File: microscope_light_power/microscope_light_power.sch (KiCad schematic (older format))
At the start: 36 parts, among them J1 MICROUSB, J2 5V175_out, J3 enable_switch, U1 MCP73871-2AA, U2 TPS61090

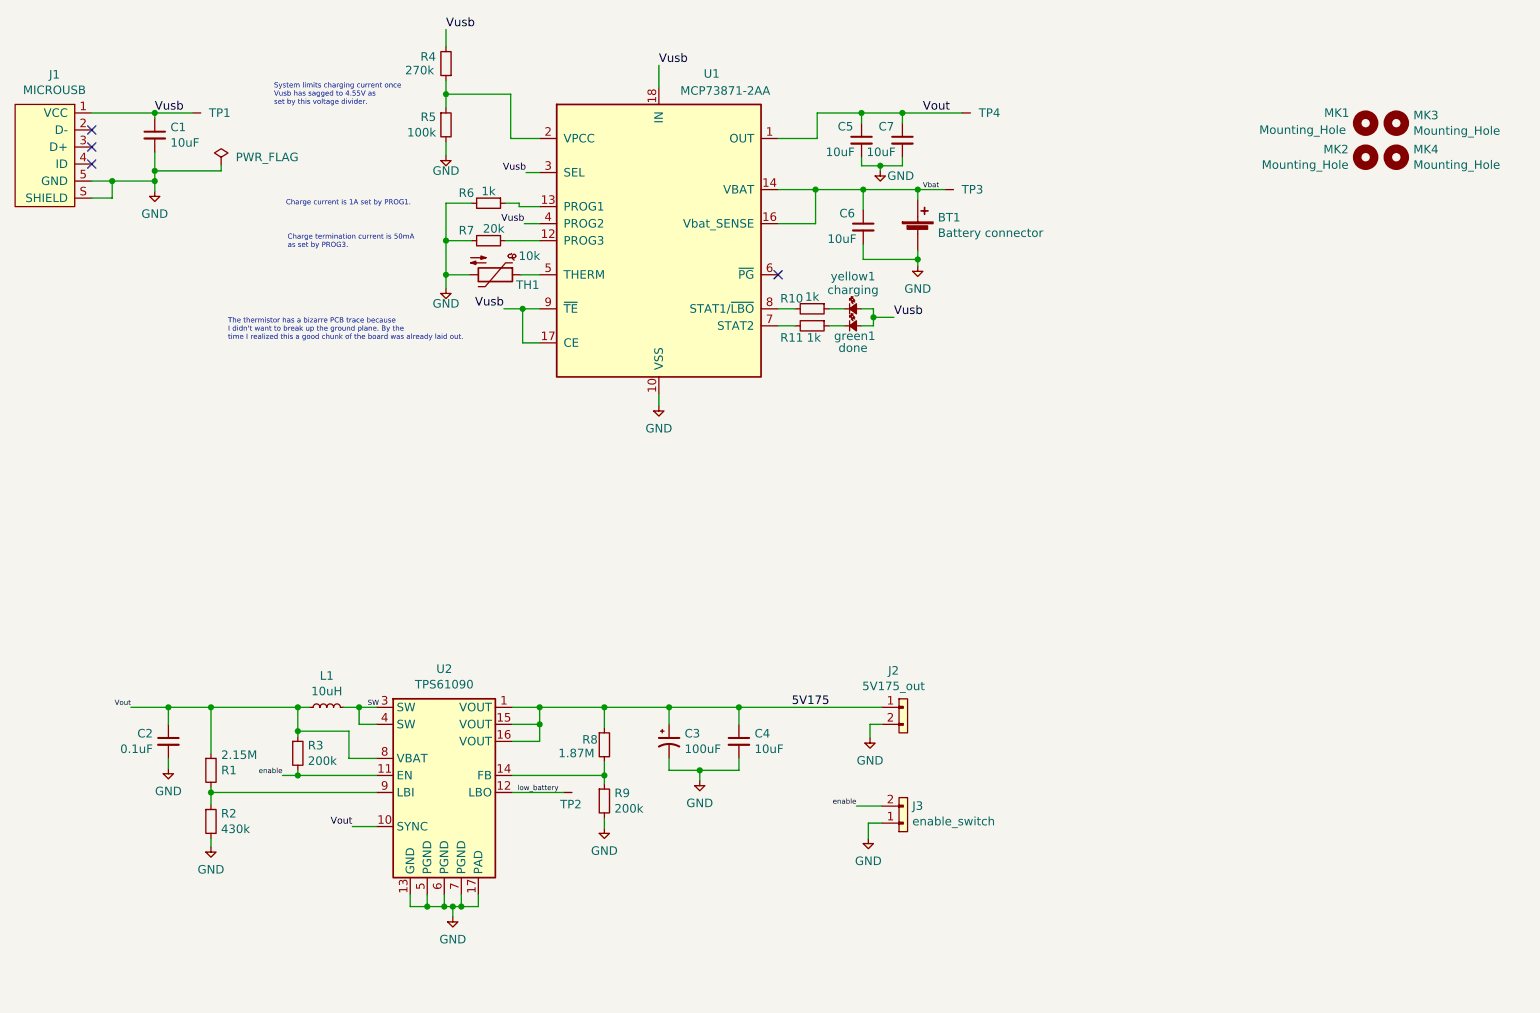
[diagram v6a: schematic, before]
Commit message: Start redoing the layout to fix some major and minor problems with this design: * The SMPS output filter caps are way too far away from the IC. This   keeps killing the internal MOSFET which fails as a short to ground   causing rapid heating and will quickly kill the battery. * The connectors weren't in very good locations. * The PCB is quite a lot bigger than it needs to be. The next rev will   a fun experiment in minituarizing this PCB! * Switch from test pads to test /throughholes/ that are a reasonable   to solder to. * Will add a second pad so the On/Off switch can be switched to normally   on or normally off.
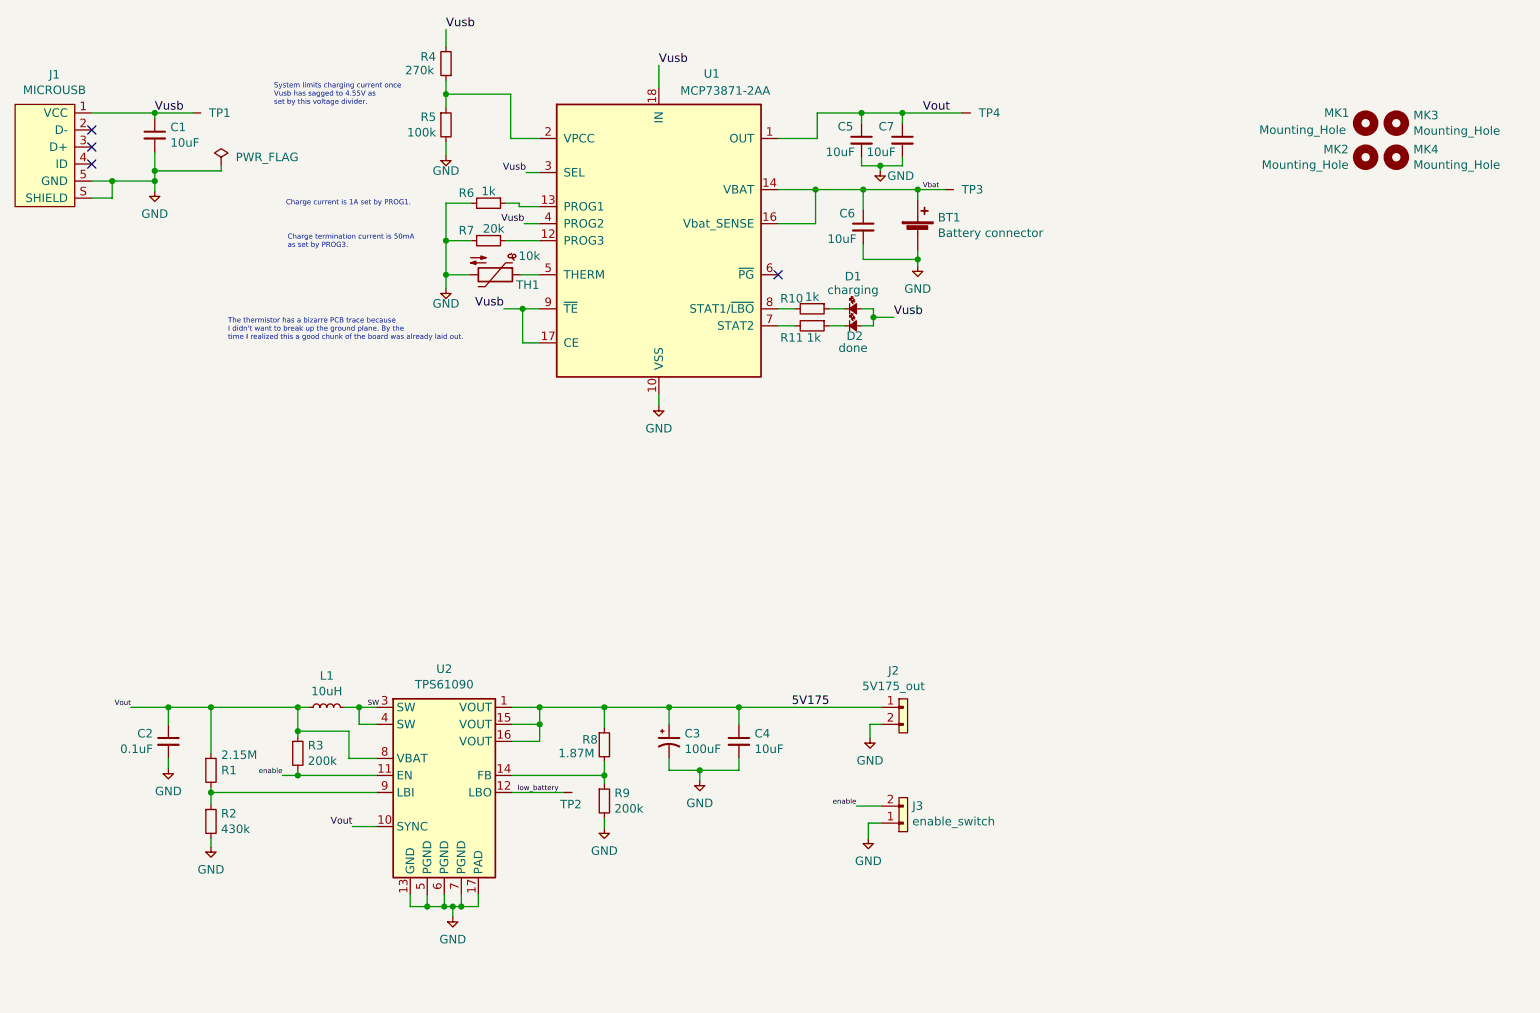
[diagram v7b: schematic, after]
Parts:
- TP1, TP3, TP4: footprint agg:TESTPAD -> Measurement_Points:Measurement_Point_Round-TH_Big
- TP2: footprint Measurement_Points:Measurement_Point_Round-TH_Small -> Measurement_Points:Measurement_Point_Round-TH_Big
- renumbered yellow1 to D1, green1 to D2
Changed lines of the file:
@@
 Vusb
 $Comp
-L agg-kicad:LED yellow1
+L agg-kicad:LED D1
 U 1 1 59DA5C71
 P 6050 2560
-F 0 "yellow1" H 6100 2750 50  0000 C CNN
+F 0 "D1" H 6100 2750 50  0000 C CNN
 F 1 "charging" H 6100 2670 50  0000 C CNN
 F 2 "LEDs:LED_0603_HandSoldering" H 6050 2560 50  0001 C CNN
@@
 $EndComp
 $Comp
-L agg-kicad:LED green1
+L agg-kicad:LED D2
 U 1 1 59DA7F2A
 P 6050 2660
-F 0 "green1" H 6110 2600 50  0000 C CNN
+F 0 "D2" H 6110 2600 50  0000 C CNN
 F 1 "done" H 6100 2530 50  0000 C CNN
 F 2 "LEDs:LED_0603_HandSoldering" H 6050 2660 50  0001 C CNN
@@
 $EndComp
 Wire Wire Line
-	1630 1410 2220 1410
+	1630 1410 2000 1410
 Wire Wire Line
 	2000 1410 2000 1440
 Wire Wire Line
-	1630 1810 2000 1810
-Wire Wire Line
-	2000 1640 2000 1870
+	1630 1810 1750 1810
+Wire Wire Line
+	2000 1640 2000 1750
 Wire Wire Line
 	1630 1910 1750 1910
@@
 	4960 1130 4960 1260
 Wire Wire Line
-	3710 1220 3710 1380
+	3710 1220 3710 1300
 Wire Wire Line
 	3710 920  3710 1020
@@
 	4260 1760 4180 1760
 Wire Wire Line
-	5660 1860 6640 1860
+	5660 1860 5880 1860
 Wire Wire Line
 	6480 1860 6480 1920
@@
 	4960 3060 4960 3130
 Wire Wire Line
-	6480 2220 6480 2310
+	6480 2220 6480 2270
 Wire Wire Line
 	6160 2180 6160 2270
@@
 	6150 2560 6220 2560
 Wire Wire Line
-	6220 2560 6220 2660
+	6220 2560 6220 2610
 Wire Wire Line
 	6220 2610 6340 2610
@@
 Connection ~ 6220 2610
 Wire Wire Line
-	4050 2560 4260 2560
+	4050 2560 4160 2560
 Wire Wire Line
 	4260 1560 4090 1560
@@
 	3860 1940 3710 1940
 Wire Wire Line
-	3710 1940 3710 2440
+	3710 1940 3710 2160
 Wire Wire Line
 	3860 2160 3710 2160
@@
 	6390 1410 6390 1470
 Wire Wire Line
-	5890 1410 6740 1410
+	5890 1410 6150 1410
 Wire Wire Line
 	6150 1410 6150 1470
@@
 	6150 1670 6150 1720
 Wire Wire Line
-	6150 1720 6390 1720
+	6150 1720 6260 1720
 Wire Wire Line
 	6390 1720 6390 1670
@@
 	3300 5600 3160 5600
 Wire Wire Line
-	3300 4900 3110 4900
+	3300 4900 3200 4900
 Wire Wire Line
 	3300 5000 3200 5000
@@
 Connection ~ 3200 4900
 Wire Wire Line
-	1860 4900 2910 4900
-Wire Wire Line
-	2840 4900 2840 5070
+	1860 4900 2080 4900
+Wire Wire Line
+	2840 4900 2840 5040
 Connection ~ 2840 4900
 Wire Wire Line
@@
 Connection ~ 2840 5040
 Wire Wire Line
-	2750 5300 3300 5300
+	2750 5300 2840 5300
 Wire Wire Line
 	2840 5300 2840 5270
@@
 Connection ~ 2330 4900
 Wire Wire Line
-	2330 5370 2330 5470
+	2330 5370 2330 5400
 Wire Wire Line
 	3300 5400 2330 5400
@@
 	4100 5400 4400 5400
 Wire Wire Line
-	4100 4900 6270 4900
+	4100 4900 4260 4900
 Wire Wire Line
 	4100 5000 4260 5000
 Wire Wire Line
-	4260 4900 4260 5100
+	4260 4900 4260 5000
 Connection ~ 4260 4900
 Wire Wire Line
@@
 Connection ~ 4640 4900
 Wire Wire Line
-	4640 5350 4640 5220
+	4640 5350 4640 5300
 Wire Wire Line
 	4640 5550 4640 5610
@@
 	5020 5200 5020 5270
 Wire Wire Line
-	5020 5270 5430 5270
+	5020 5270 5200 5270
 Wire Wire Line
 	5430 5270 5430 5200
@@
 F 0 "TP2" H 4380 5330 50  0000 L CNN
 F 1 "TESTPAD" H 4400 5325 50  0001 L CNN
-F 2 "Measurement_Points:Measurement_Point_Round-TH_Small" H 4400 5250 50  0001 L CNN
+F 2 "Measurement_Points:Measurement_Point_Round-TH_Big" H 4400 5250 50  0001 L CNN
 F 3 "" H 4400 5400 50  0001 C CNN
 	1    4400 5400
@@
 F 0 "TP4" H 6838 1410 50  0000 L CNN
 F 1 "TESTPAD" H 6740 1335 50  0001 L CNN
-F 2 "agg:TESTPAD" H 6740 1260 50  0001 L CNN
+F 2 "Measurement_Points:Measurement_Point_Round-TH_Big" H 6740 1260 50  0001 L CNN
 F 3 "" H 6740 1410 50  0001 C CNN
 	1    6740 1410
@@
 F 0 "TP1" H 2318 1410 50  0000 L CNN
 F 1 "TESTPAD" H 2220 1335 50  0001 L CNN
-F 2 "agg:TESTPAD" H 2220 1260 50  0001 L CNN
+F 2 "Measurement_Points:Measurement_Point_Round-TH_Big" H 2220 1260 50  0001 L CNN
 F 3 "" H 2220 1410 50  0001 C CNN
 	1    2220 1410
@@
 F 0 "TP3" H 6738 1860 50  0000 L CNN
 F 1 "TESTPAD" H 6640 1785 50  0001 L CNN
-F 2 "agg:TESTPAD" H 6640 1710 50  0001 L CNN
+F 2 "Measurement_Points:Measurement_Point_Round-TH_Big" H 6640 1710 50  0001 L CNN
 F 3 "" H 6640 1860 50  0001 C CNN
 	1    6640 1860
@@
 	3500 6000 3500 6070
 Wire Wire Line
-	3500 6070 3900 6070
+	3500 6070 3600 6070
 Wire Wire Line
 	3900 6070 3900 6000
@@
 	1    0    0    -1
 $EndComp
+Wire Wire Line
+	1750 1810 2000 1810
+Wire Wire Line
+	2000 1810 2000 1870
+Wire Wire Line
+	5880 1860 6160 1860
+Wire Wire Line
+	6160 1860 6480 1860
+Wire Wire Line
+	6480 2270 6480 2310
+Wire Wire Line
+	6220 2610 6220 2660
+Wire Wire Line
+	3710 1300 3710 1380
+Wire Wire Line
+	3710 2160 3710 2360
+Wire Wire Line
+	4160 2560 4260 2560
+Wire Wire Line
+	3710 2360 3710 2440
+Wire Wire Line
+	6150 1410 6390 1410
+Wire Wire Line
+	6390 1410 6740 1410
+Wire Wire Line
+	6260 1720 6390 1720
+Wire Wire Line
+	3200 4900 3110 4900
+Wire Wire Line
+	2840 4900 2910 4900
+Wire Wire Line
+	2840 5040 2840 5070
+Wire Wire Line
+	2840 5300 3300 5300
+Wire Wire Line
+	2330 4900 2840 4900
+Wire Wire Line
+	2330 5400 2330 5470
+Wire Wire Line
+	4260 4900 4640 4900
+Wire Wire Line
+	4260 5000 4260 5100
+Wire Wire Line
+	4640 4900 5020 4900
+Wire Wire Line
+	4640 5300 4640 5220
+Wire Wire Line
+	2080 4900 2330 4900
+Wire Wire Line
+	5430 4900 6270 4900
+Wire Wire Line
+	5020 4900 5430 4900
+Wire Wire Line
+	5200 5270 5430 5270
+Wire Wire Line
+	2000 1410 2220 1410
+Wire Wire Line
+	6480 1860 6640 1860
+Wire Wire Line
+	2000 1750 2000 1810
+Wire Wire Line
+	3600 6070 3700 6070
+Wire Wire Line
+	3700 6070 3750 6070
+Wire Wire Line
+	3800 6070 3900 6070
+Wire Wire Line
+	3750 6070 3800 6070
 $EndSCHEMATC

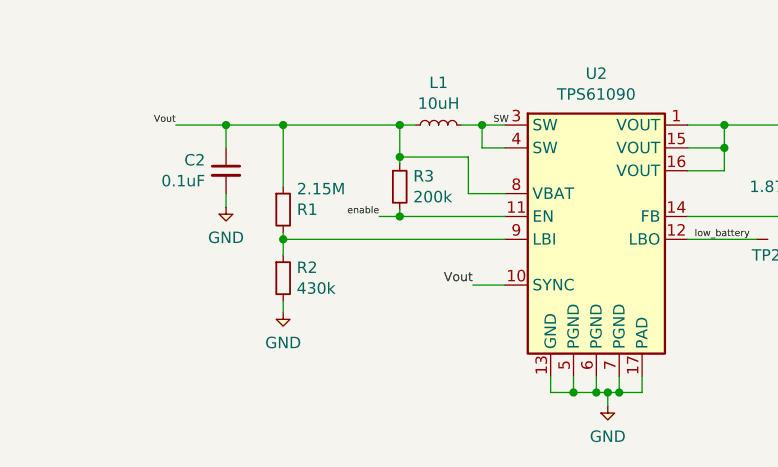
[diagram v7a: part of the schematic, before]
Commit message: Add resistors to select normally on/normally off output. Scrunch in more components, shift things around a bit, etc etc.
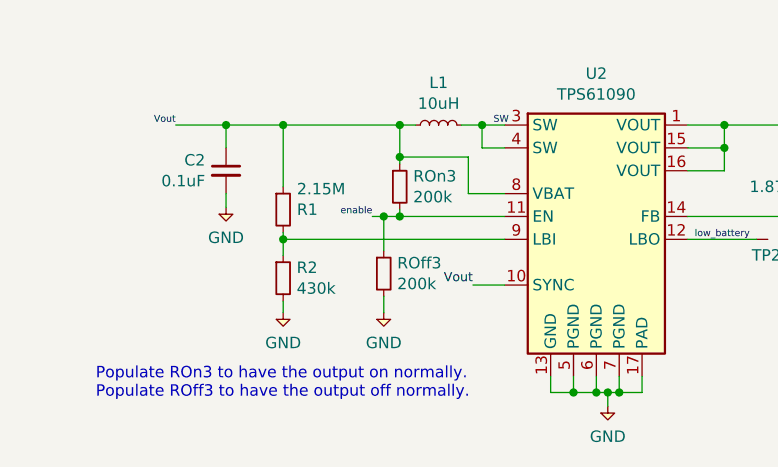
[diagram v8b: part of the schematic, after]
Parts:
- added ROff3: 200k, Resistors_SMD:R_0603_HandSoldering, symbol device:R_Small
- renumbered R3 to ROn3
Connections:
- net GND: now also ROff3.2
- net enable: now also ROff3.1
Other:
- note added: "Populate ROn3 to have the output on normally.\nPopulate ROff3 to have the output off normally."
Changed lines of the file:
@@
 Vout
 $Comp
-L device:R_Small R3
+L device:R_Small ROn3
 U 1 1 59EE2E52
 P 2840 5170
-F 0 "R3" H 2899 5216 50  0000 L CNN
+F 0 "ROn3" H 2899 5216 50  0000 L CNN
 F 1 "200k" H 2899 5125 50  0000 L CNN
 F 2 "Resistors_SMD:R_0603_HandSoldering" H 2840 5170 50  0001 C CNN
@@
 	1    0    0    -1
 $EndComp
-Text Label 2750 5300 2    30   ~ 0
+Text Label 2720 5300 2    30   ~ 0
 enable
 $Comp
@@
 Connection ~ 2840 5040
 Wire Wire Line
-	2750 5300 2840 5300
-Wire Wire Line
 	2840 5300 2840 5270
 Connection ~ 2840 5300
@@
 Wire Wire Line
 	3750 6070 3800 6070
+$Comp
+L device:R_Small ROff3
+U 1 1 5B1032CA
+P 2770 5550
+F 0 "ROff3" H 2829 5596 50  0000 L CNN
+F 1 "200k" H 2829 5505 50  0000 L CNN
+F 2 "Resistors_SMD:R_0603_HandSoldering" H 2770 5550 50  0001 C CNN
+F 3 "" H 2770 5550 50  0001 C CNN
+	1    2770 5550
+	1    0    0    -1
+$EndComp
+Wire Wire Line
+	2770 5450 2770 5300
+Connection ~ 2770 5300
+Wire Wire Line
+	2770 5300 2840 5300
+Wire Wire Line
+	2720 5300 2770 5300
+$Comp
+L agg-kicad:GND #PWR0101
+U 1 1 5B1121D5
+P 2770 5720
+F 0 "#PWR0101" H 2640 5760 50  0001 L CNN
+F 1 "GND" H 2770 5587 50  0000 C CNN
+F 2 "" H 2770 5720 50  0001 C CNN
+F 3 "" H 2770 5720 50  0001 C CNN
+	1    2770 5720
+	1    0    0    -1
+$EndComp
+Wire Wire Line
+	2770 5650 2770 5720
+Text Notes 1510 6100 0    50   ~ 0
+Populate ROn3 to have the output on normally.\nPopulate ROff3 to have the output off normally.
 $EndSCHEMATC
